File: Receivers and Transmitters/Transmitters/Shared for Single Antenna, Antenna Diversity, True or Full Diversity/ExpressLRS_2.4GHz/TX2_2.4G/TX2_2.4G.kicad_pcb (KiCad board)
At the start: 4 copper layers, 39.8 x 55.8 mm, 11 parts, among them J1 Conn_01x05_Socket, J2 Conn_01x03_Socket, J3 Conn_01x04_Socket, U1 TPS7A4701xRGW, U2 ESP32-WROOM-32, U3 E28-2G4M27S

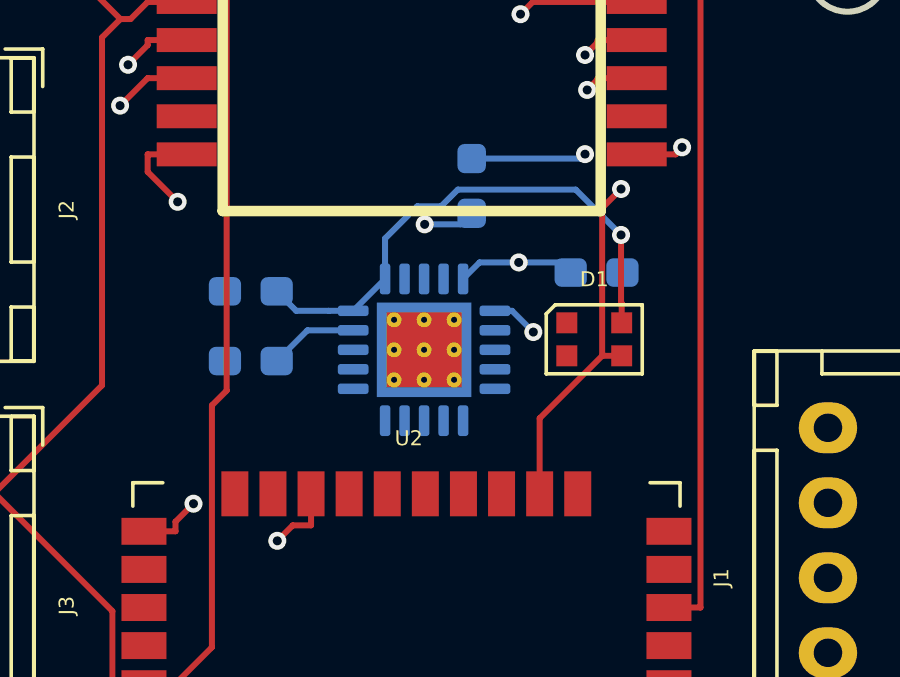
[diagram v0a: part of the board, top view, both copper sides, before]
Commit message: Fixed incorrect LED RGB connection to ESP32 on TX2_2.4G and TX3_2.4G schematics and PCBs
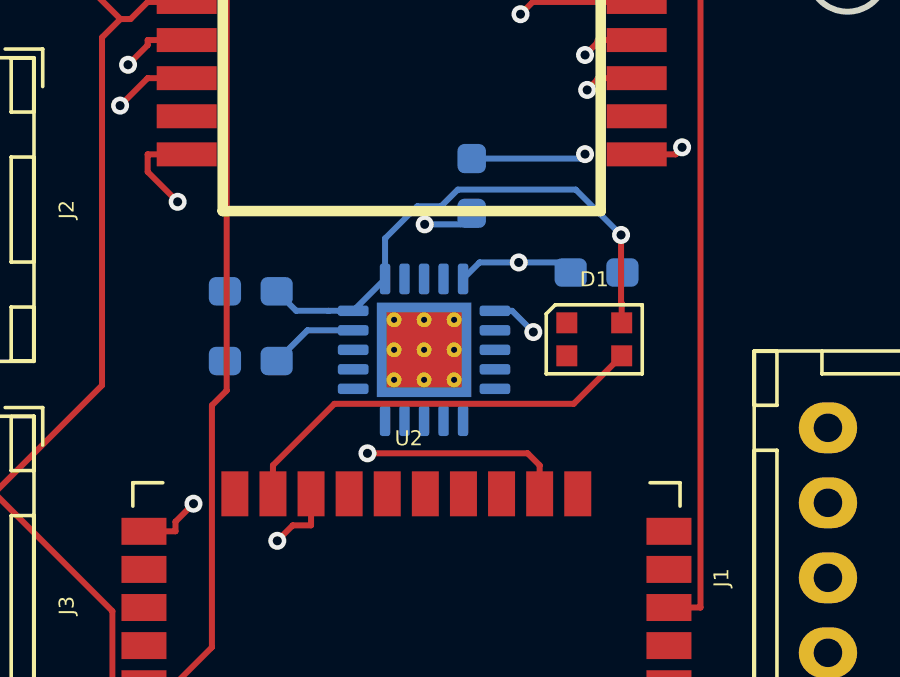
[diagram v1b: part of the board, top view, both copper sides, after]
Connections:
- D1 pad 3: /SPORT -> /LED_RGB
- U2 pad 23: unconnected-(U2-IO15-Pad23) -> /LED_RGB
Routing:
- net /LED_RGB: track 0.00 -> 14.1 mm
- net /SPORT: track 34.7 -> 24.8 mm
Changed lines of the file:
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@@
 			(psa4output no)
 			(plot_black_and_white yes)
-			(plotinvisibletext no)
 			(sketchpadsonfab no)
 			(plotpadnumbers no)
@@
 	(net 40 "unconnected-(U2-IO17-Pad28)")
 	(net 41 "/NRESET")
-	(net 42 "unconnected-(U2-IO15-Pad23)")
+	(net 42 "/LED_RGB")
 	(net 43 "unconnected-(U2-NC-Pad32)")
 	(net 44 "/DIO1")
@@
 			(size 0.7 0.7)
 			(layers "F.Cu" "F.Mask" "F.Paste")
-			(net 6 "/SPORT")
+			(net 42 "/LED_RGB")
 			(pinfunction "DIN")
 			(pintype "input")
@@
 			(size 1.5 0.9)
 			(layers "F.Cu" "F.Mask" "F.Paste")
-			(net 42 "unconnected-(U2-IO15-Pad23)")
+			(net 42 "/LED_RGB")
 			(pinfunction "IO15")
-			(pintype "bidirectional+no_connect")
+			(pintype "bidirectional")
 		)
 		(pad "24" smd rect
@@
 	)
 	(segment
-		(start 155.9983 81.55)
-		(end 155.9983 76.6196)
-		(width 0.2)
-		(layer "F.Cu")
-		(net 6)
-	)
-	(segment
-		(start 155.9983 76.6196)
-		(end 156.6283 75.9896)
-		(width 0.2)
-		(layer "F.Cu")
-		(net 6)
-	)
-	(segment
-		(start 153.915 86.15)
-		(end 153.915 83.6333)
+		(start 153.915 85.2)
+		(end 153.915 86.15)
 		(width 0.2)
 		(layer "F.Cu")
@@
 	)
 	(segment
-		(start 153.915 83.6333)
-		(end 155.9983 81.55)
+		(start 153.515 84.8)
+		(end 153.915 85.2)
 		(width 0.2)
 		(layer "F.Cu")
@@
 	)
 	(segment
-		(start 156.65 81.55)
-		(end 155.9983 81.55)
+		(start 148.175 84.8)
+		(end 153.515 84.8)
 		(width 0.2)
 		(layer "F.Cu")
@@
 	)
 	(via
-		(at 156.6283 75.9896)
+		(at 148.175 84.8)
 		(size 0.6)
 		(drill 0.3)
@@
 	)
 	(segment
-		(start 156.6283 75.9896)
-		(end 156.4539 75.8152)
+		(start 139.1902 75.8152)
+		(end 136.2402 75.8152)
 		(width 0.2)
 		(layer "In1.Cu")
@@
 	)
 	(segment
-		(start 136.2402 75.8152)
-		(end 134.6 74.175)
+		(start 148.175 84.8)
+		(end 139.1902 75.8152)
 		(width 0.2)
 		(layer "In1.Cu")
@@
 	)
 	(segment
-		(start 156.4539 75.8152)
-		(end 136.2402 75.8152)
+		(start 136.2402 75.8152)
+		(end 134.6 74.175)
 		(width 0.2)
 		(layer "In1.Cu")
@@
 		(net 37)
 	)
+	(segment
+		(start 147.075 83.15)
+		(end 155.05 83.15)
+		(width 0.2)
+		(layer "F.Cu")
+		(net 42)
+	)
+	(segment
+		(start 155.05 83.15)
+		(end 156.65 81.55)
+		(width 0.2)
+		(layer "F.Cu")
+		(net 42)
+	)
+	(segment
+		(start 145.025 85.2)
+		(end 147.075 83.15)
+		(width 0.2)
+		(layer "F.Cu")
+		(net 42)
+	)
+	(segment
+		(start 145.025 86.15)
+		(end 145.025 85.2)
+		(width 0.2)
+		(layer "F.Cu")
+		(net 42)
+	)
 	(zone
